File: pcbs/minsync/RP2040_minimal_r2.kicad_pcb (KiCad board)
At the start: 2 copper layers, 42 x 42 mm, 43 parts, among them J1 SWD_JST, J5 SWD_HEADERS, J6 Conn_01x01_Pin, J7 SSD1306, SW1 SW_Push, U1 NCP1117-3.3_SOT223, U2 W25Q128JVS, U3 RP2040, U4 Si5351A-B-GT, Y2 Crystal_GND24

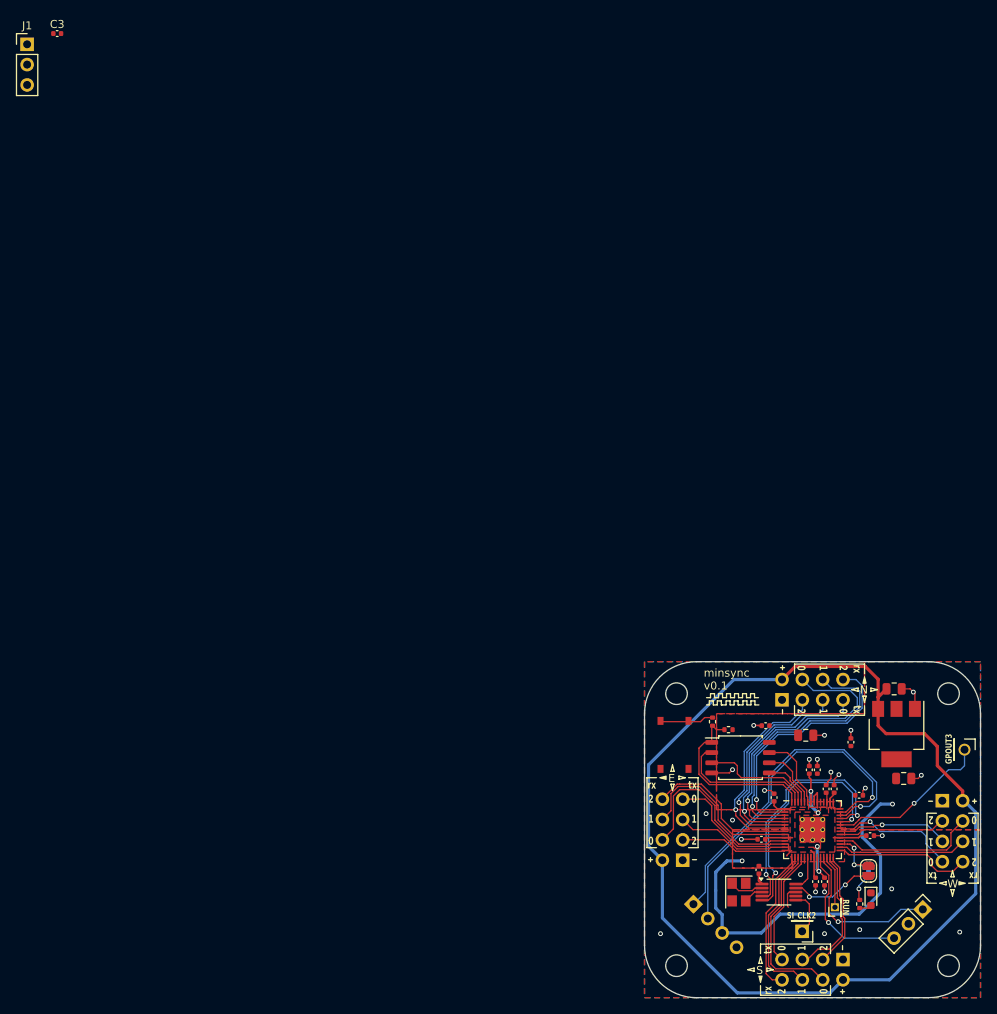
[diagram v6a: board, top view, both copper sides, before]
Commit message: minsync: Implement fixes for problems in v0.1, bump version to v0.2.
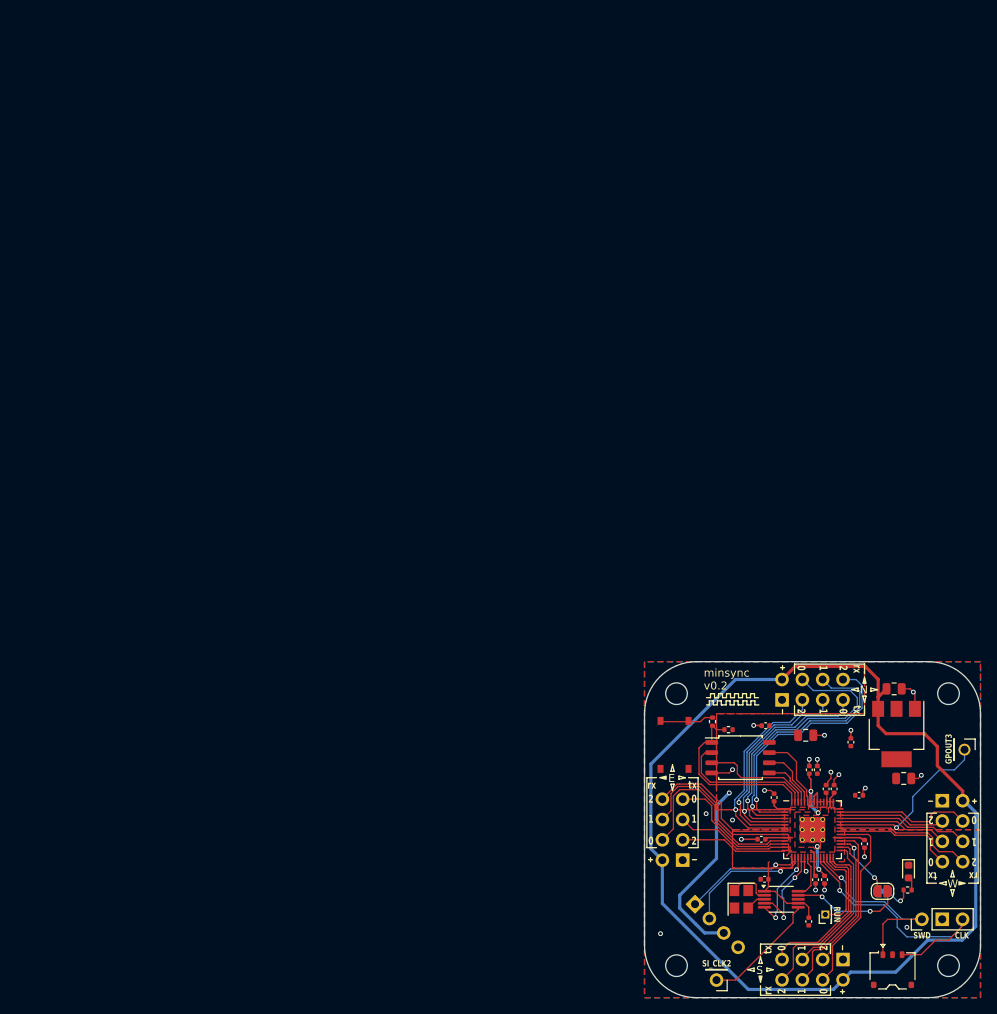
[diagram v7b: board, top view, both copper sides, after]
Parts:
- J1: footprint Connector_PinHeader_2.54mm:PinHeader_1x03_P2.54mm_Vertical -> Connector_JST:JST_ACH_BM03B-ACHSS-GAN-ETF_1x03-1MP_P1.20mm_Vertical
- moved J1 158.4 mm to (110.0, 117.5)
- moved C3 145.4 mm to (99.5, 111.5), turned to -90 degrees
- moved TP2 12.3 mm to (88.0, 118.8)
- moved R3 6.24 mm to (111.9, 107.5), turned to 180 degrees
- moved D1 5.83 mm to (112.0, 105.2)
- moved JP1 3.09 mm to (108.8, 107.7), turned to 180 degrees
- moved JP2 3.09 mm to (108.8, 107.7), turned to 180 degrees
- moved J6 1.50 mm to (101.6, 110.6)
- moved C2 1.37 mm to (94.0, 106.2), turned to 180 degrees
- moved J5 1.24 mm to (113.7, 111.2), turned to 90 degrees
- moved C12 1.24 mm to (106.5, 101.8), turned to -90 degrees
- moved U4 0.95 mm to (96.1, 108.7)
- moved Y2 0.95 mm to (91.1, 108.7)
- moved C14 0.23 mm to (100.4, 106.2)
- moved C7 0.23 mm to (101.5, 106.2)
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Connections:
- J7 pad 1: /GPIO28_ADC2 -> /GPIO12
- J7 pad 2: /GPIO29_ADC3 -> /GPIO13
- PTP3 pad 3: /GPIO17 -> /GPIO21
- PTP3 pad 4: /GPIO14 -> /GPIO22
- PTP3 pad 5: /GPIO16 -> /GPIO18
- PTP3 pad 6: /GPIO13 -> /GPIO19
- PTP3 pad 7: /GPIO15 -> /GPIO16
- PTP3 pad 8: /GPIO12 -> /GPIO17
- PTP4 pad 3: /GPIO22 -> /GPIO28_ADC2
- PTP4 pad 4: /GPIO21 -> /GPIO29_ADC3
- PTP4 pad 5: /GPIO23 -> /GPIO26_ADC0
- PTP4 pad 6: /GPIO19 -> /GPIO27_ADC1
- PTP4 pad 7: /GPIO24 -> /GPIO23
- PTP4 pad 8: /GPIO18 -> /GPIO24
- U4 pad 4: /GPIO27_ADC1 -> /GPIO15
- U4 pad 5: /GPIO26_ADC0 -> /GPIO14
- Y2 pad 2: GND -> unconnected-(Y2-Pad2)
- Y2 pad 4: GND -> unconnected-(Y2-Pad4)
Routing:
- net /GPIO28_ADC2: track 44.0 -> 13.5 mm, vias 1 -> 0
- net /GPIO29_ADC3: track 43.3 -> 17.1 mm, vias 1 -> 0
- net /GPIO26_ADC0: track 30.1 -> 13.8 mm, vias 2 -> 0
- net /SWCLK: track 18.0 -> 34.1 mm
- net +3V3: track 70.9 -> 56.5 mm, vias 2 -> 1
- net /GPIO27_ADC1: track 30.8 -> 16.5 mm, vias 2 -> 0
- net /GPIO14: track 22.0 -> 10.7 mm, vias 0 -> 2
- net /GPIO22: track 13.6 -> 24.3 mm
- net /SI_CLK2: track 5.67 -> 14.7 mm
- net /GPIO17: track 14.5 -> 22.4 mm
- net /SWD: track 20.3 -> 25.5 mm
- net /GPIO19: track 16.2 -> 21.3 mm
- net /RUN: track 6.68 -> 11.1 mm
- net /GPIO13: track 19.9 -> 16.2 mm, vias 0 -> 1
- net /GPIO16: track 16.7 -> 20.1 mm
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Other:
- board text added: "CLK"
- board text added: "SWD"
- board text added: "minsync v0.2"
- board text removed: "minsync v0.1"

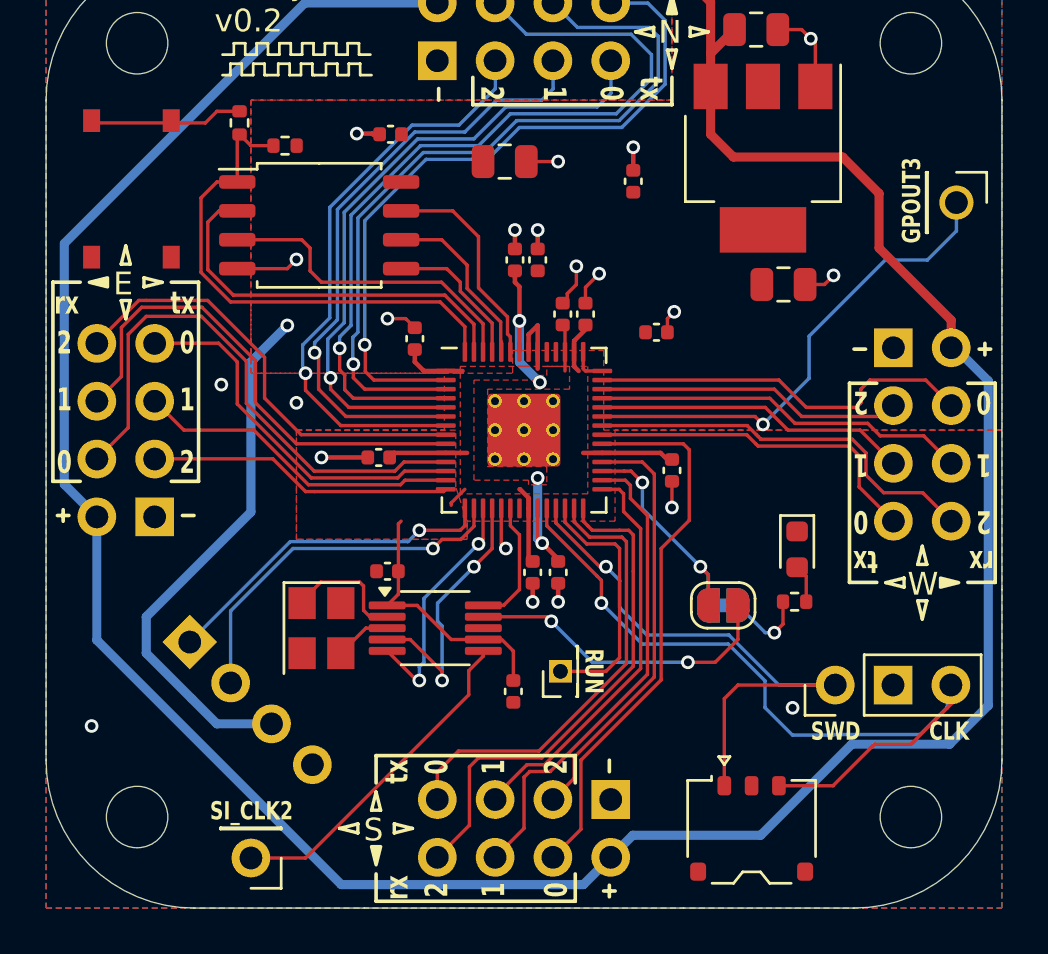
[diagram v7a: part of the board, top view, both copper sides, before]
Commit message: Add pullups for si5351, change SWD plug footprint
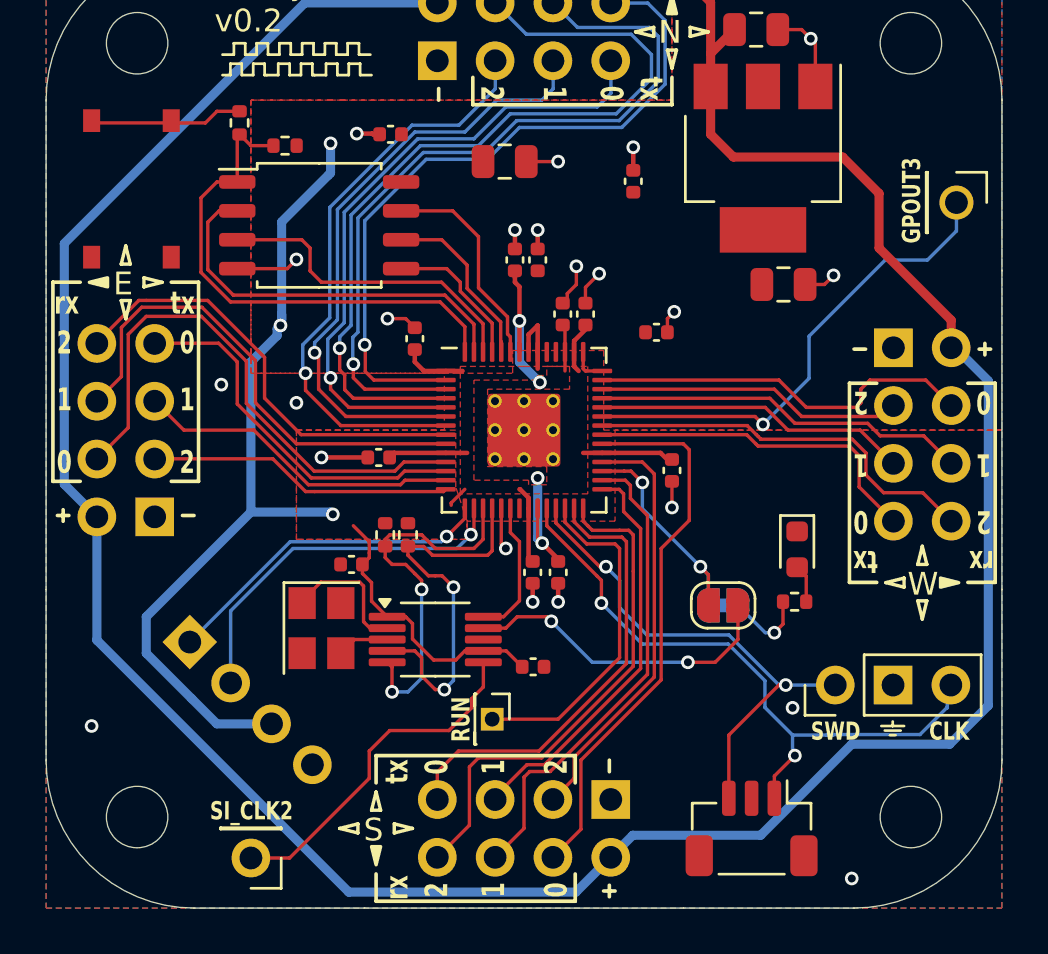
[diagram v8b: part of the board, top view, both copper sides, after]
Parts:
- added R4: 4.7k, Resistor_SMD:R_0402_1005Metric, F.Cu at (93.9, 104.6)
- added R5: 4.7k, Resistor_SMD:R_0402_1005Metric, F.Cu at (94.9, 104.6)
- J1: footprint Connector_JST:JST_ACH_BM03B-ACHSS-GAN-ETF_1x03-1MP_P1.20mm_Vertical -> Connector_JST:JST_SH_BM03B-SRSS-TB_1x03-1MP_P1.00mm_Vertical
- moved J6 3.66 mm to (98.6, 112.7), turned to -90 degrees
- moved C2 1.61 mm to (92.4, 105.9)
- moved C3 1.39 mm to (100.4, 110.4), turned to 0 degrees
- moved U4 0.50 mm to (96.1, 109.2)
- turned J1 to 180 degrees
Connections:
- J1 pad 1: /SWD -> /SWCLK
- J1 pad 3: /SWCLK -> /SWD
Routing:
- net +3V3: track 56.5 -> 70.8 mm, vias 1 -> 3
- net /SWCLK: track 34.1 -> 28.2 mm, vias 1 -> 2
- net /GPIO14: track 10.7 -> 16.2 mm
- net /GPIO15: track 12.0 -> 17.1 mm
- net /RUN: track 11.1 -> 15.0 mm
- net /SWD: track 25.5 -> 22.8 mm, vias 1 -> 2
- net /SI_CLK2: track 14.7 -> 15.3 mm
- net /XA: track 5.44 -> 5.94 mm
- net GND: vias 21 -> 22
